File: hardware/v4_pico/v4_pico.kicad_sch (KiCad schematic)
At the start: 102 parts, among them J1 joystick, J10 ON/OFF, J11 MIDI IN bk: 5 R: 4, J2 LED strip, J3 SSD1306 SPI, J4 MIDI OUT Y:M5 - R:M4, J5 Batt, J6 Neck - Y:O BK:B R:3.3, J7 01x03, J8 MXP5010, J9 Thumb, Q1 2N7000, SW1 SW_DIP_x01, U1 74HC165, U2 74HC165, U3 74HC165, U4 Pico, U5 FJ08K, U6 6N138, U7 MCP3002

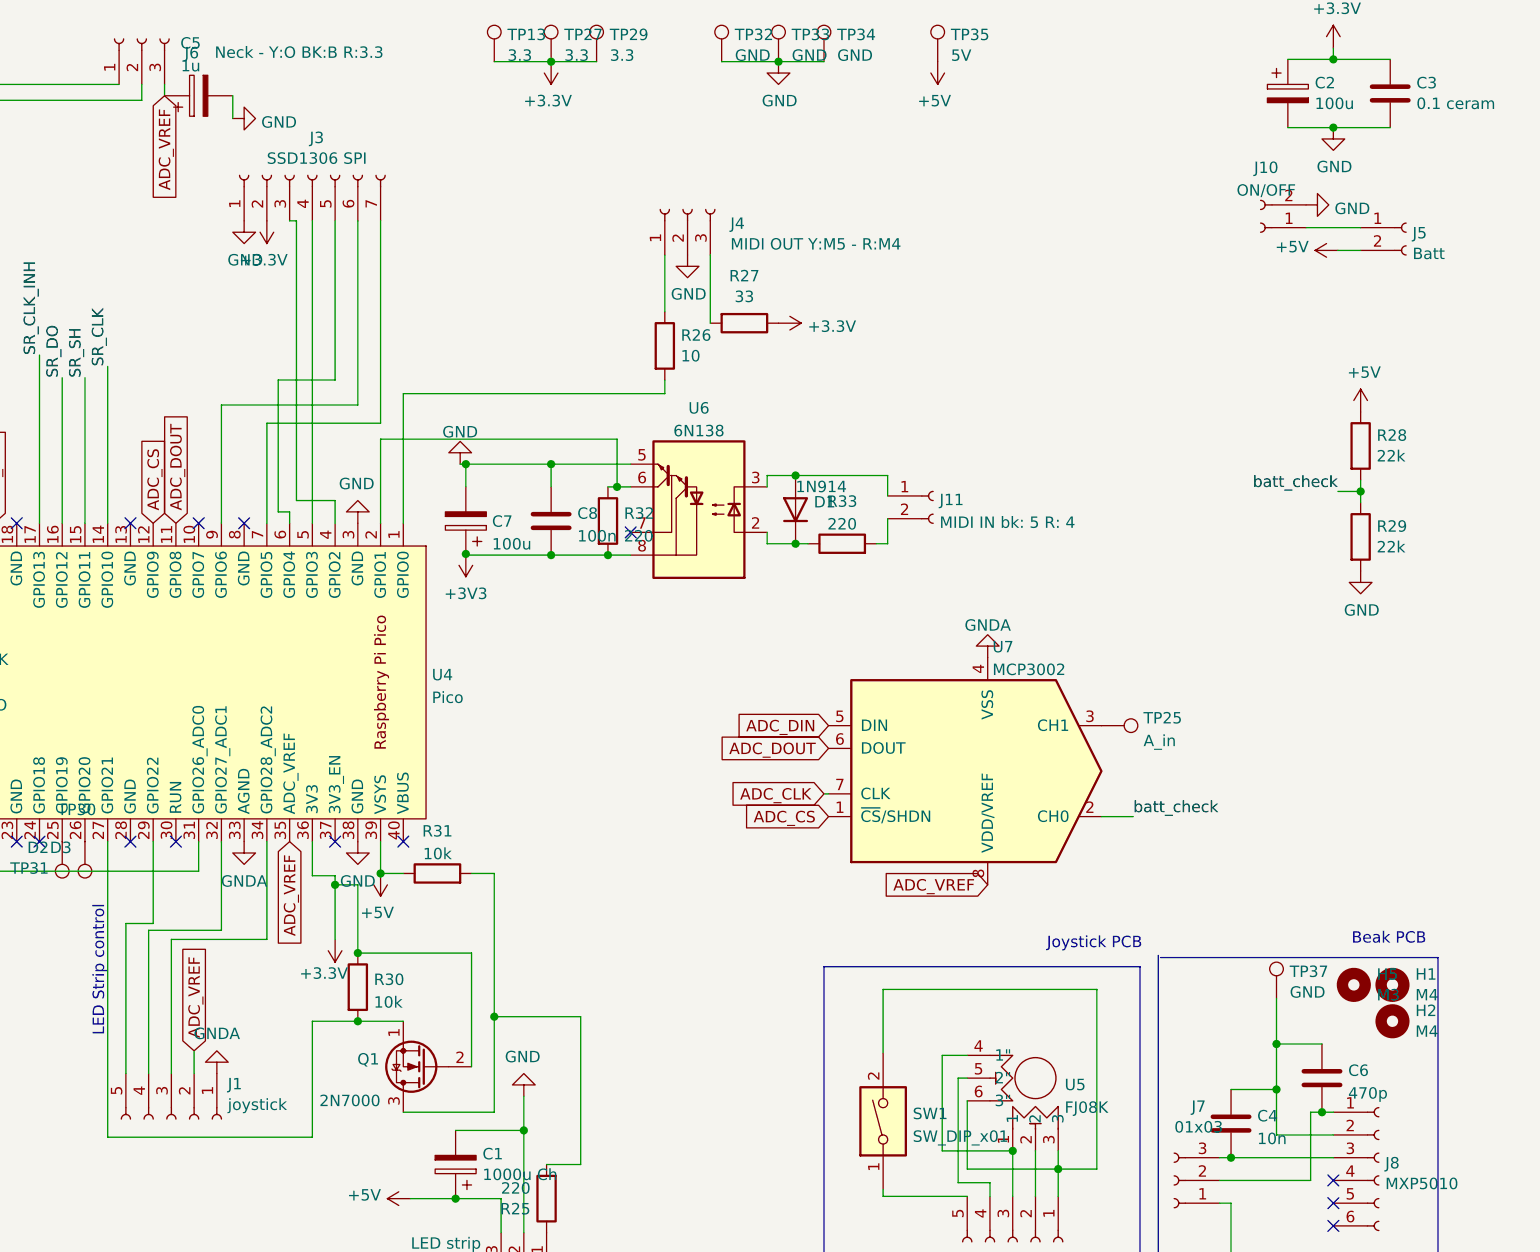
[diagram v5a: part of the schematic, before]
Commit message: Corrected scheme for DRC«
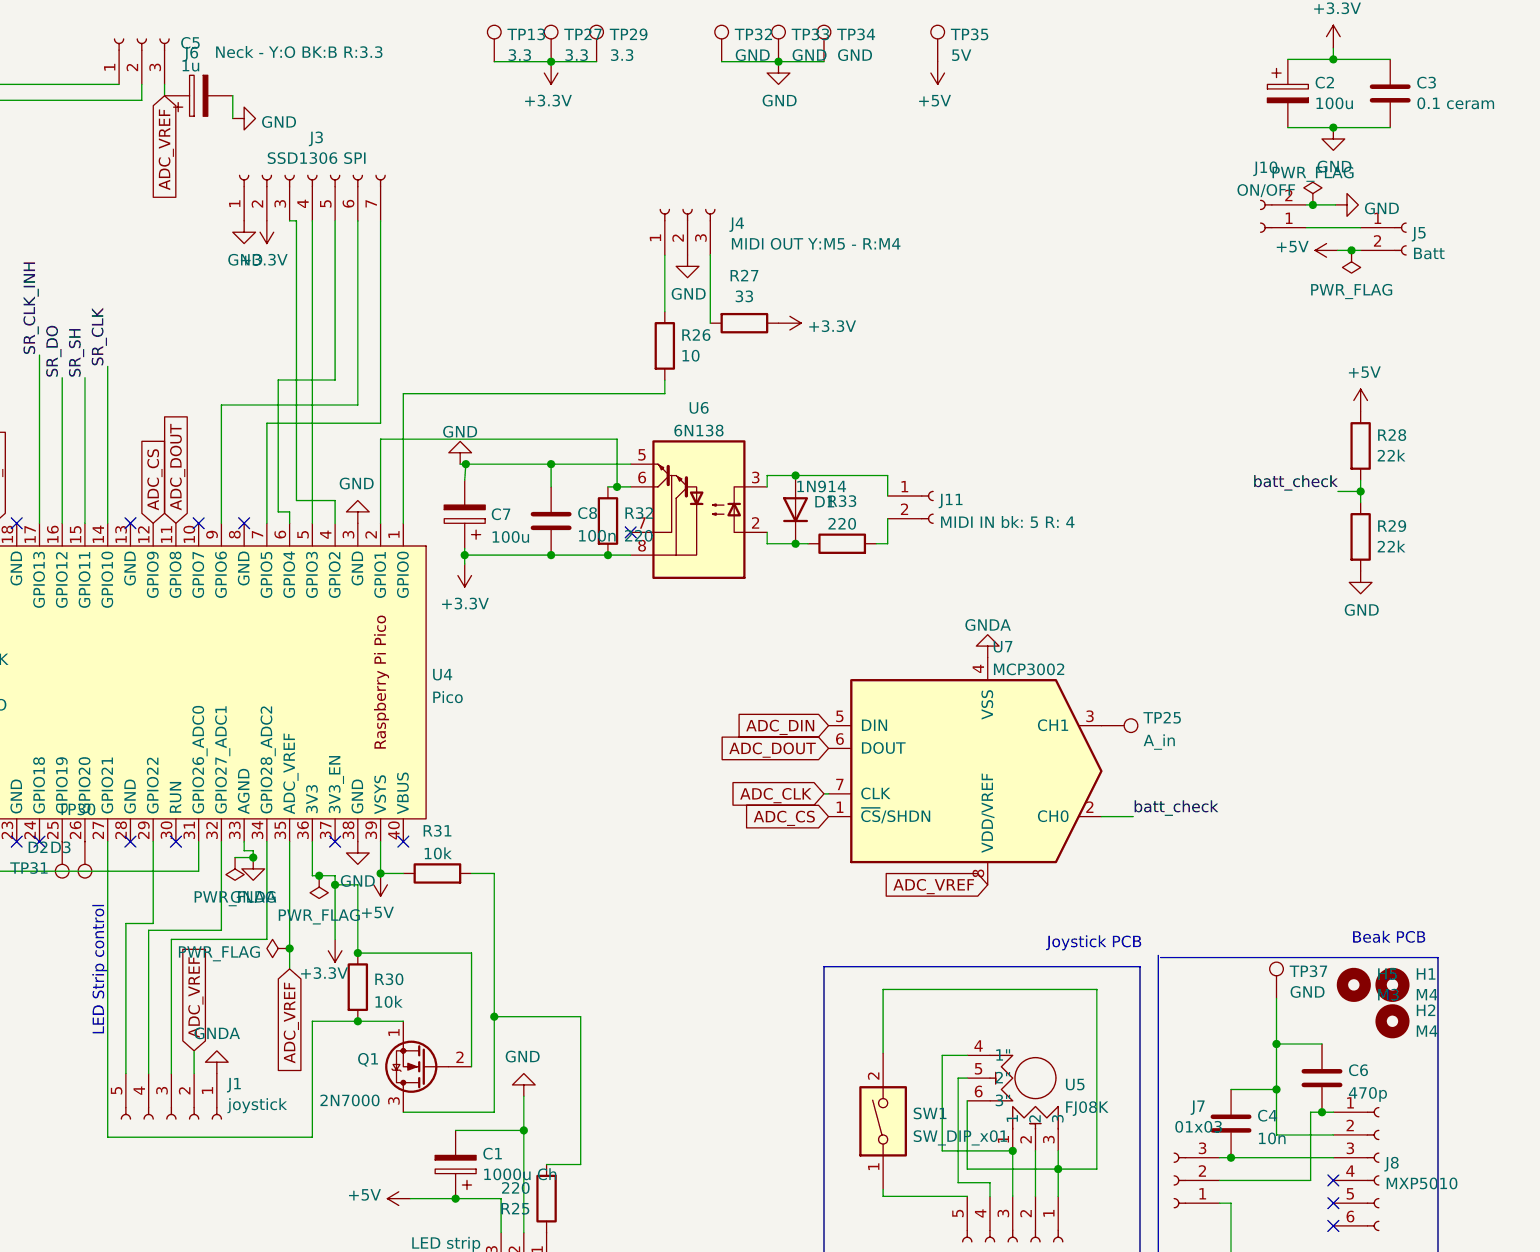
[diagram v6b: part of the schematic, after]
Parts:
- Q1: footprint Package_TO_SOT_THT:TO-92_HandSolder -> Package_TO_SOT_THT:TO-92_Inline
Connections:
- net +3V3 is gone; now on net +3.3V: C2.1, C3.1, J3.2 (Pin_2), Q1.2 (G), R1.2, R10.2, R11.2, R12.2, R13.2, R14.2, R15.2, R16.2, R17.2, R18.2, R19.2, R2.2, R20.2, R21.2, R22.2, R23.2, R24.2, R27.1, R3.2, R30.1, R4.2, R5.2, R6.2, R7.2, R8.2, R9.2, TP13.1, TP27.1, TP29.1, U1.16 (VCC), U2.16 (VCC), U3.16 (VCC), U4.36 (3V3)
- net +3.3V: now reaches C7.1, C8.2, R32.2, U6.8 (VCC)
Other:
- moved on the sheet: C7

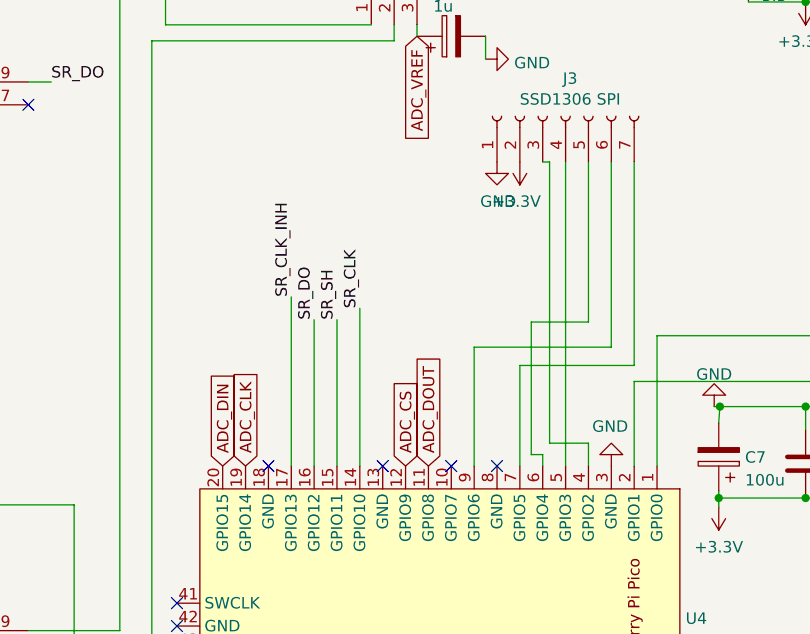
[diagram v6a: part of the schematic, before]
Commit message: Moved adc and screen to same bus
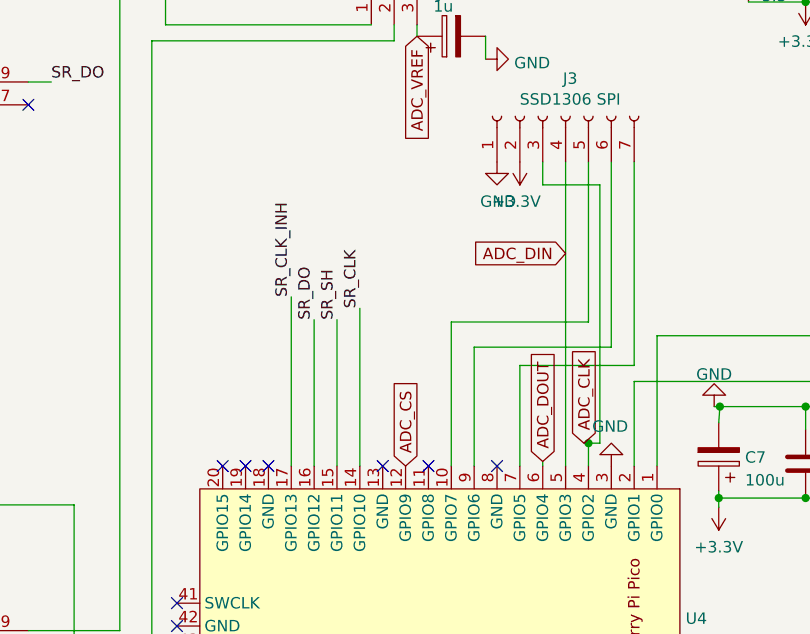
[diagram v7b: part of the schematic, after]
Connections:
- net ADC_CLK: now also J3.3 (Pin_3), U4.4 (GPIO2); no longer U4.19 (GPIO14)
- net ADC_DIN: now also J3.4 (Pin_4), U4.5 (GPIO3); no longer U4.20 (GPIO15)
- net ADC_DOUT: now also U4.6 (GPIO4); no longer U4.11 (GPIO8)
- net at J3.5 (Pin_5): now also U4.10 (GPIO7); no longer U4.6 (GPIO4)
- no-connect marks 23 -> 25
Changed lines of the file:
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@@
   (junction (at 49.53 165.1) (diameter 0) (color 0 0 0 0)
+  )
+  (junction (at 160.02 70.612) (diameter 0) (color 0 0 0 0)
   )
   (junction (at 48.26 96.52) (diameter 0) (color 0 0 0 0)
@@
   (no_connect (at 97.79 33.02))
   (no_connect (at 160.02 108.712))
+  (no_connect (at 142.24 73.152))
   (no_connect (at 119.38 108.712))
   (no_connect (at 114.3 93.472))
+  (no_connect (at 119.38 73.152))
   (no_connect (at 124.46 73.152))
-  (no_connect (at 144.78 73.152))
   (no_connect (at 137.16 73.152))
   (no_connect (at 97.79 157.48))
@@
   (no_connect (at 142.24 108.712))
   (no_connect (at 114.3 88.392))
+  (no_connect (at 121.92 73.152))
   (no_connect (at 97.79 93.98))
   (no_connect (at 127 108.712))
@@
     (stroke (width 0) (type default) (color 0 0 0 0))
   )
+  (wire (pts (xy 154.94 72.644) (xy 154.94 73.152))
+    (stroke (width 0) (type default) (color 0 0 0 0))
+  )
   (wire (pts (xy 72.39 77.47) (xy 102.87 77.47))
     (stroke (width 0) (type default) (color 0 0 0 0))
@@
     (stroke (width 0) (type default) (color 0 0 0 0))
   )
+  (wire (pts (xy 159.512 70.612) (xy 160.02 70.612))
+    (stroke (width 0) (type default) (color 0 0 0 0))
+  )
   (wire (pts (xy 57.15 43.18) (xy 36.83 43.18))
     (stroke (width 0) (type default) (color 0 0 0 0))
@@
     (stroke (width 0) (type default) (color 0 0 0 0))
   )
-  (wire (pts (xy 153.67 57.15) (xy 160.02 57.15))
+  (wire (pts (xy 144.78 57.15) (xy 160.02 57.15))
     (stroke (width 0) (type default) (color 0 0 0 0))
   )
@@
     (stroke (width 0) (type default) (color 0 0 0 0))
   )
-  (wire (pts (xy 155.702 39.37) (xy 155.702 70.612))
+  (wire (pts (xy 161.29 41.91) (xy 161.29 70.612))
     (stroke (width 0) (type default) (color 0 0 0 0))
   )
@@
     (stroke (width 0) (type default) (color 0 0 0 0))
   )
-  (wire (pts (xy 153.67 71.882) (xy 153.67 57.15))
-    (stroke (width 0) (type default) (color 0 0 0 0))
-  )
   (wire (pts (xy 67.31 93.98) (xy 72.39 93.98))
     (stroke (width 0) (type default) (color 0 0 0 0))
@@
     (stroke (width 0) (type default) (color 0 0 0 0))
   )
+  (wire (pts (xy 144.78 57.15) (xy 144.78 73.152))
+    (stroke (width 0) (type default) (color 0 0 0 0))
+  )
   (wire (pts (xy 211.455 75.438) (xy 212.852 75.438))
     (stroke (width 0) (type default) (color 0 0 0 0))
@@
     (stroke (width 0) (type default) (color 0 0 0 0))
   )
-  (wire (pts (xy 155.702 39.37) (xy 154.94 39.37))
+  (wire (pts (xy 161.29 41.91) (xy 154.94 41.91))
     (stroke (width 0) (type default) (color 0 0 0 0))
   )
@@
     (stroke (width 0) (type default) (color 0 0 0 0))
   )
+  (wire (pts (xy 154.94 41.91) (xy 154.94 39.37))
+    (stroke (width 0) (type default) (color 0 0 0 0))
+  )
   (wire (pts (xy 230.632 145.288) (xy 240.792 145.288))
     (stroke (width 0) (type default) (color 0 0 0 0))
@@
     (stroke (width 0) (type default) (color 0 0 0 0))
   )
-  (wire (pts (xy 154.94 73.152) (xy 154.94 71.882))
-    (stroke (width 0) (type default) (color 0 0 0 0))
-  )
   (wire (pts (xy 221.234 148.336) (xy 221.234 147.574))
     (stroke (width 0) (type default) (color 0 0 0 0))
@@
     (stroke (width 0) (type default) (color 0 0 0 0))
   )
-  (wire (pts (xy 155.702 70.612) (xy 160.02 70.612))
+  (wire (pts (xy 161.29 70.612) (xy 160.02 70.612))
     (stroke (width 0) (type default) (color 0 0 0 0))
   )
@@
   )
   (wire (pts (xy 17.78 63.5) (xy 43.18 63.5))
-    (stroke (width 0) (type default) (color 0 0 0 0))
-  )
-  (wire (pts (xy 154.94 71.882) (xy 153.67 71.882))
     (stroke (width 0) (type default) (color 0 0 0 0))
   )
@@
     )
   )
+  (global_label "ADC_DOUT" (shape input) (at 154.94 72.644 90) (fields_autoplaced)
+    (effects (font (size 1.27 1.27)) (justify left))
+    (property "Références Inter-Feuilles" "${INTERSHEET_REFS}" (id 0) (at 154.8606 60.825 90)
+      (effects (font (size 1.27 1.27)) (justify left) hide)
+    )
+  )
   (global_label "ADC_DIN" (shape input) (at 215.138 95.758 180) (fields_autoplaced)
     (effects (font (size 1.27 1.27)) (justify right))
@@
     )
   )
-  (global_label "ADC_DIN" (shape input) (at 119.38 73.152 90) (fields_autoplaced)
+  (global_label "ADC_DIN" (shape input) (at 157.48 49.53 180) (fields_autoplaced)
+    (effects (font (size 1.27 1.27)) (justify right))
+    (property "Références Inter-Feuilles" "${INTERSHEET_REFS}" (id 0) (at 147.3544 49.6094 0)
+      (effects (font (size 1.27 1.27)) (justify right) hide)
+    )
+  )
+  (global_label "ADC_CLK" (shape input) (at 159.512 70.612 90) (fields_autoplaced)
     (effects (font (size 1.27 1.27)) (justify left))
-    (property "Références Inter-Feuilles" "${INTERSHEET_REFS}" (id 0) (at 119.3006 63.0264 90)
-      (effects (font (size 1.27 1.27)) (justify left) hide)
-    )
-  )
-  (global_label "ADC_DOUT" (shape input) (at 142.24 73.152 90) (fields_autoplaced)
-    (effects (font (size 1.27 1.27)) (justify left))
-    (property "Références Inter-Feuilles" "${INTERSHEET_REFS}" (id 0) (at 142.1606 61.333 90)
+    (property "Références Inter-Feuilles" "${INTERSHEET_REFS}" (id 0) (at 159.4326 60.1235 90)
       (effects (font (size 1.27 1.27)) (justify left) hide)
     )
@@
     )
   )
-  (global_label "ADC_CLK" (shape input) (at 121.92 73.152 90) (fields_autoplaced)
-    (effects (font (size 1.27 1.27)) (justify left))
-    (property "Références Inter-Feuilles" "${INTERSHEET_REFS}" (id 0) (at 121.8406 62.6635 90)
-      (effects (font (size 1.27 1.27)) (justify left) hide)
-    )
-  )

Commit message: Updated footprints
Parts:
- U1, U2, U3: footprint Package_DIP:DIP-16_W7.62mm_Socket -> Package_SO:SOIC-16_3.9x9.9mm_P1.27mm
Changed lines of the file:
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@@
     (property "Reference" "U1" (id 0) (at 85.09 18.2626 0))
     (property "Value" "74HC165" (id 1) (at 85.09 20.574 0))
-    (property "Footprint" "Package_DIP:DIP-16_W7.62mm_Socket" (id 2) (at 85.09 45.72 0)
+    (property "Footprint" "Package_SO:SOIC-16_3.9x9.9mm_P1.27mm" (id 2) (at 85.09 45.72 0)
       (effects (font (size 1.27 1.27)) hide)
     )
@@
     (property "Reference" "U2" (id 0) (at 85.09 79.2226 0))
     (property "Value" "74HC165" (id 1) (at 85.09 81.534 0))
-    (property "Footprint" "Package_DIP:DIP-16_W7.62mm_Socket" (id 2) (at 85.09 106.68 0)
+    (property "Footprint" "Package_SO:SOIC-16_3.9x9.9mm_P1.27mm" (id 2) (at 85.09 106.68 0)
       (effects (font (size 1.27 1.27)) hide)
     )
@@
     (property "Reference" "U3" (id 0) (at 85.09 142.7226 0))
     (property "Value" "74HC165" (id 1) (at 85.09 145.034 0))
-    (property "Footprint" "Package_DIP:DIP-16_W7.62mm_Socket" (id 2) (at 85.09 170.18 0)
+    (property "Footprint" "Package_SO:SOIC-16_3.9x9.9mm_P1.27mm" (id 2) (at 85.09 170.18 0)
       (effects (font (size 1.27 1.27)) hide)
     )
@@
     )
     (path "/00000000-0000-0000-0000-000061b1bb58"
-      (reference "U1") (unit 1) (value "74HC165") (footprint "Package_DIP:DIP-16_W7.62mm_Socket")
+      (reference "U1") (unit 1) (value "74HC165") (footprint "Package_SO:SOIC-16_3.9x9.9mm_P1.27mm")
     )
     (path "/00000000-0000-0000-0000-000061b1cfb1"
-      (reference "U2") (unit 1) (value "74HC165") (footprint "Package_DIP:DIP-16_W7.62mm_Socket")
+      (reference "U2") (unit 1) (value "74HC165") (footprint "Package_SO:SOIC-16_3.9x9.9mm_P1.27mm")
     )
     (path "/00000000-0000-0000-0000-000061b1d538"
-      (reference "U3") (unit 1) (value "74HC165") (footprint "Package_DIP:DIP-16_W7.62mm_Socket")
+      (reference "U3") (unit 1) (value "74HC165") (footprint "Package_SO:SOIC-16_3.9x9.9mm_P1.27mm")
     )
     (path "/548a6b39-284d-44c8-9c5c-d9af1c8c3533"
